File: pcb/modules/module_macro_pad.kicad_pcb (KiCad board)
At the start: 2 copper layers, 80.5 x 19 mm, 9 parts

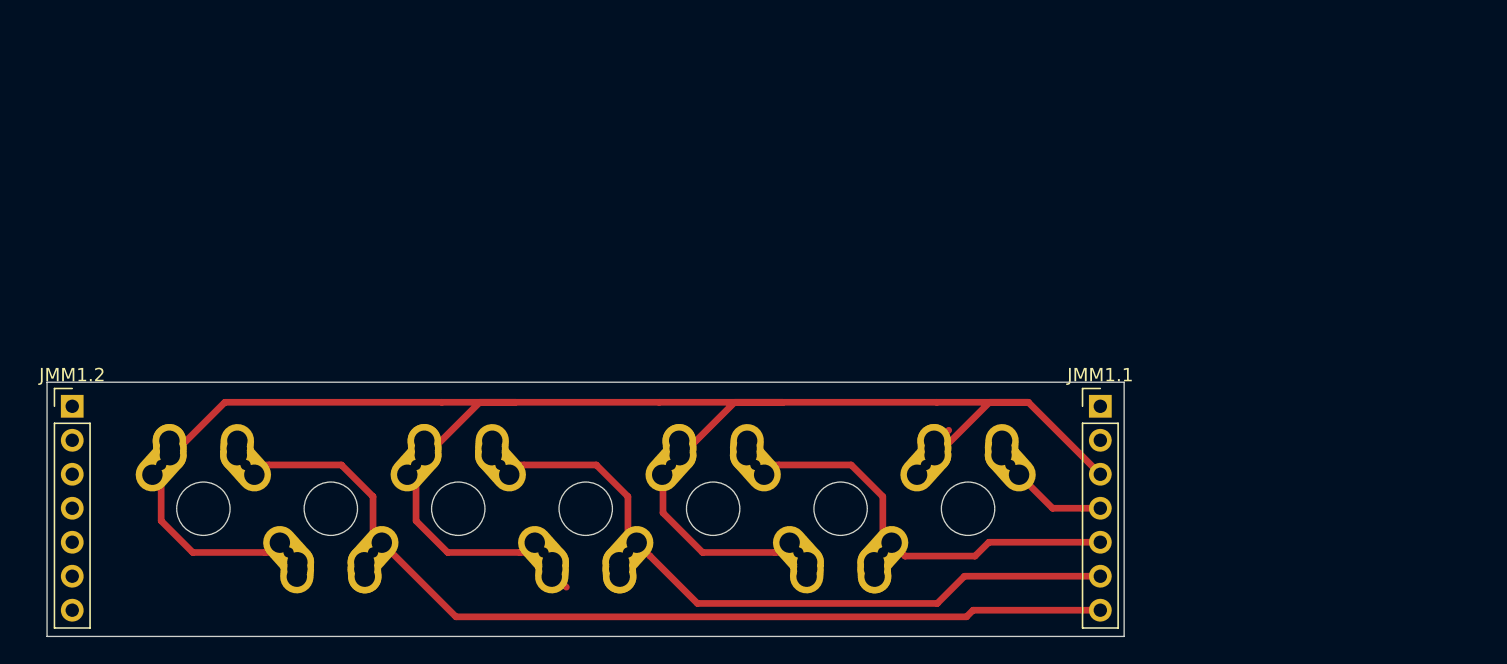
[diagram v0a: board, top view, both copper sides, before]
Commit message: Upadeted modular pcb project and moved them to modules folder
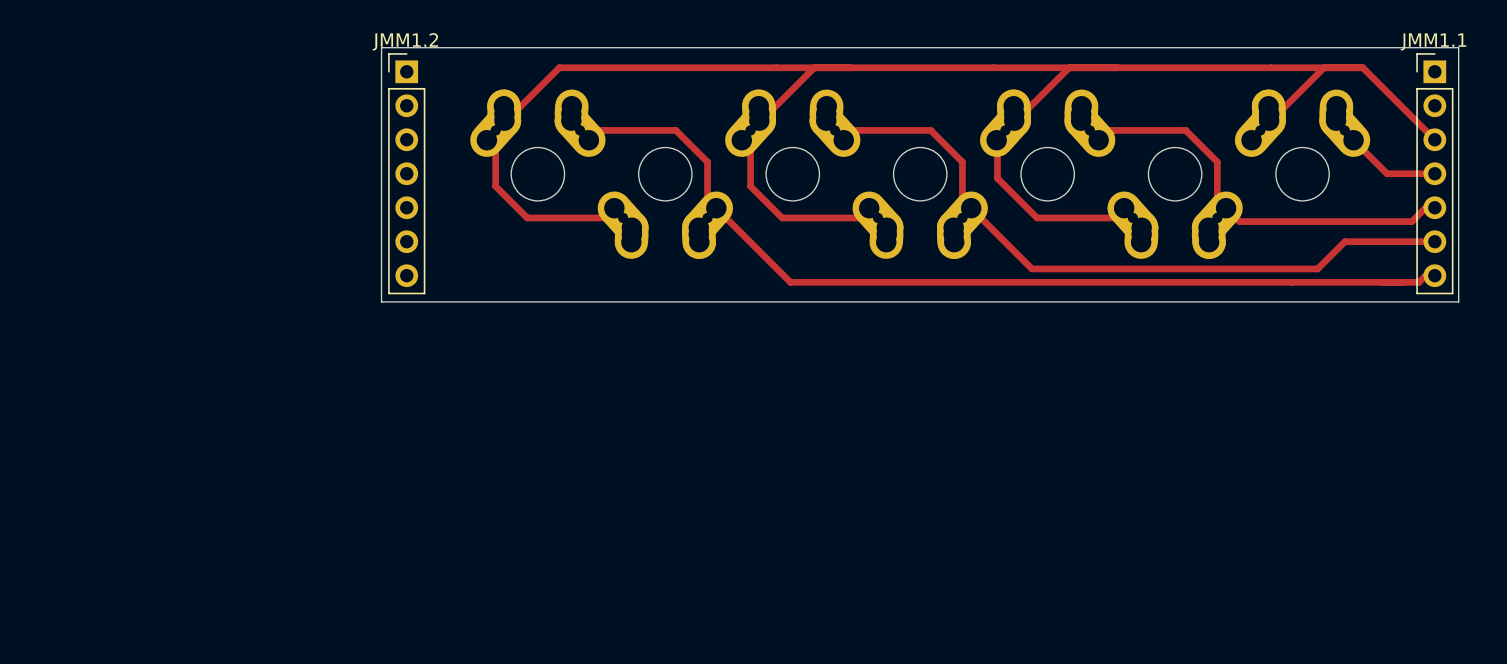
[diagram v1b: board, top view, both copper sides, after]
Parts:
- moved JMM1.1 35.4 mm to (222.5, 6.70)
- moved JMM1.2 35.4 mm to (145.6, 6.70)
- moved SWA7.2 35.4 mm to (212.6, 14.3)
- moved SWB7.1 35.4 mm to (193.5, 14.3)
- moved SWB7.2 35.4 mm to (203.1, 14.3)
- moved SWC7.1 35.4 mm to (174.5, 14.3)
- moved SWC7.2 35.4 mm to (184.0, 14.3)
- moved SWD7.1 35.4 mm to (155.4, 14.3)
- moved SWD7.2 35.4 mm to (165.0, 14.3)
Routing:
- net Net-(JMM1.1-Pad3): track 156.0 -> 153.0 mm
- net Net-(JMM1.1-Pad7): track 70.9 -> 72.6 mm
